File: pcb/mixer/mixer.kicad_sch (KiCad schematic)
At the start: 17 parts, among them J1 Conn_01x02_Pin, J4 Conn_Coaxial, J5 Conn_Coaxial, J6 AudioJack3, J7 AudioJack3, P1 PMOD-Device-x2-Type-Generic-A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, U17 LT1117-3.3, U3 Si5351C-B-GU, U5 LT1117-5.0, X8 TCXO-14

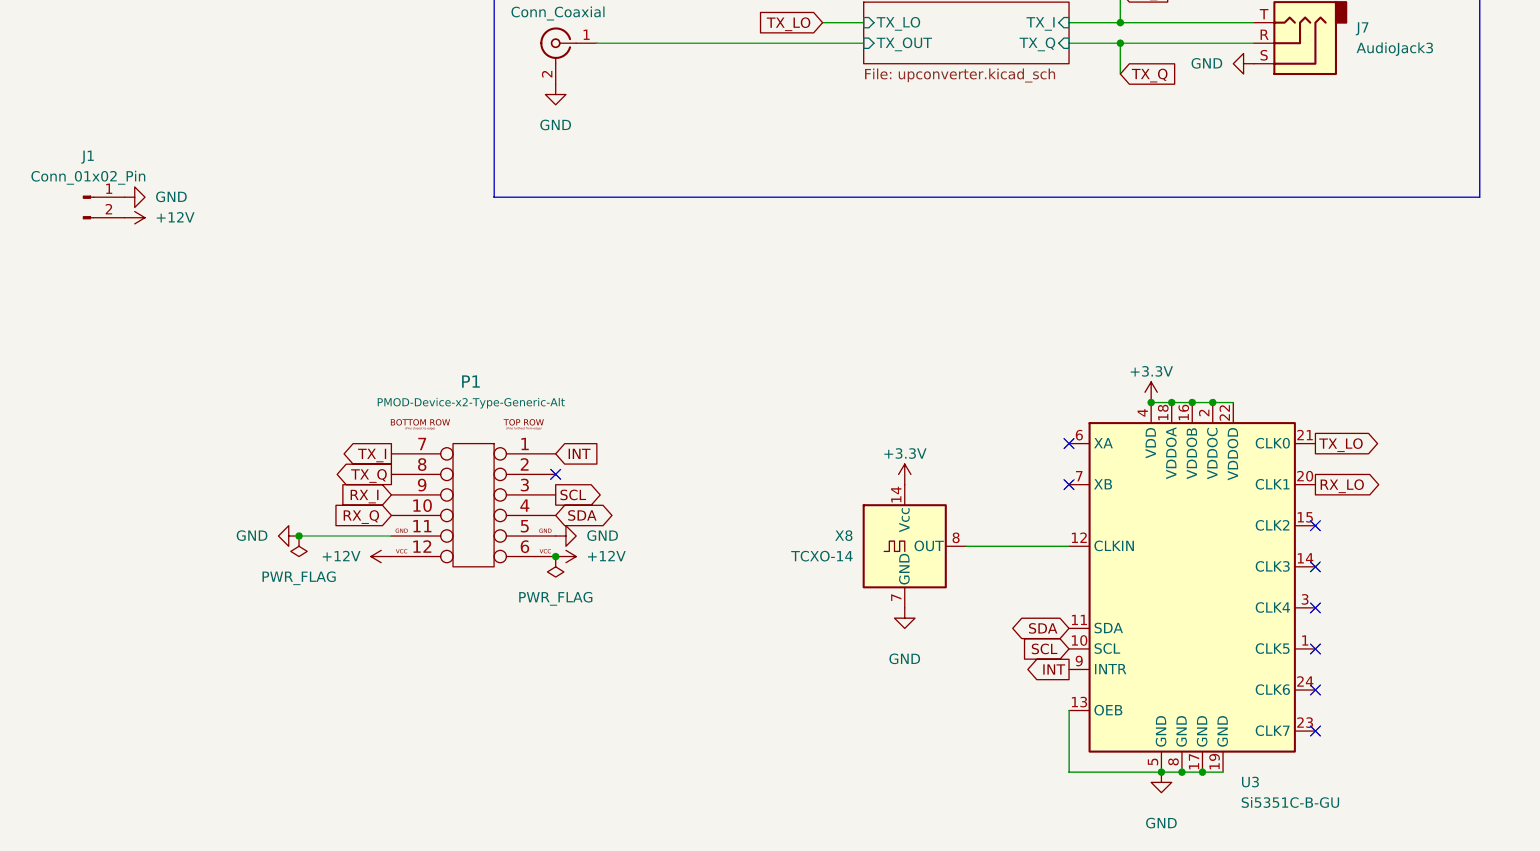
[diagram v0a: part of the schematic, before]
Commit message: add README.md from external repository
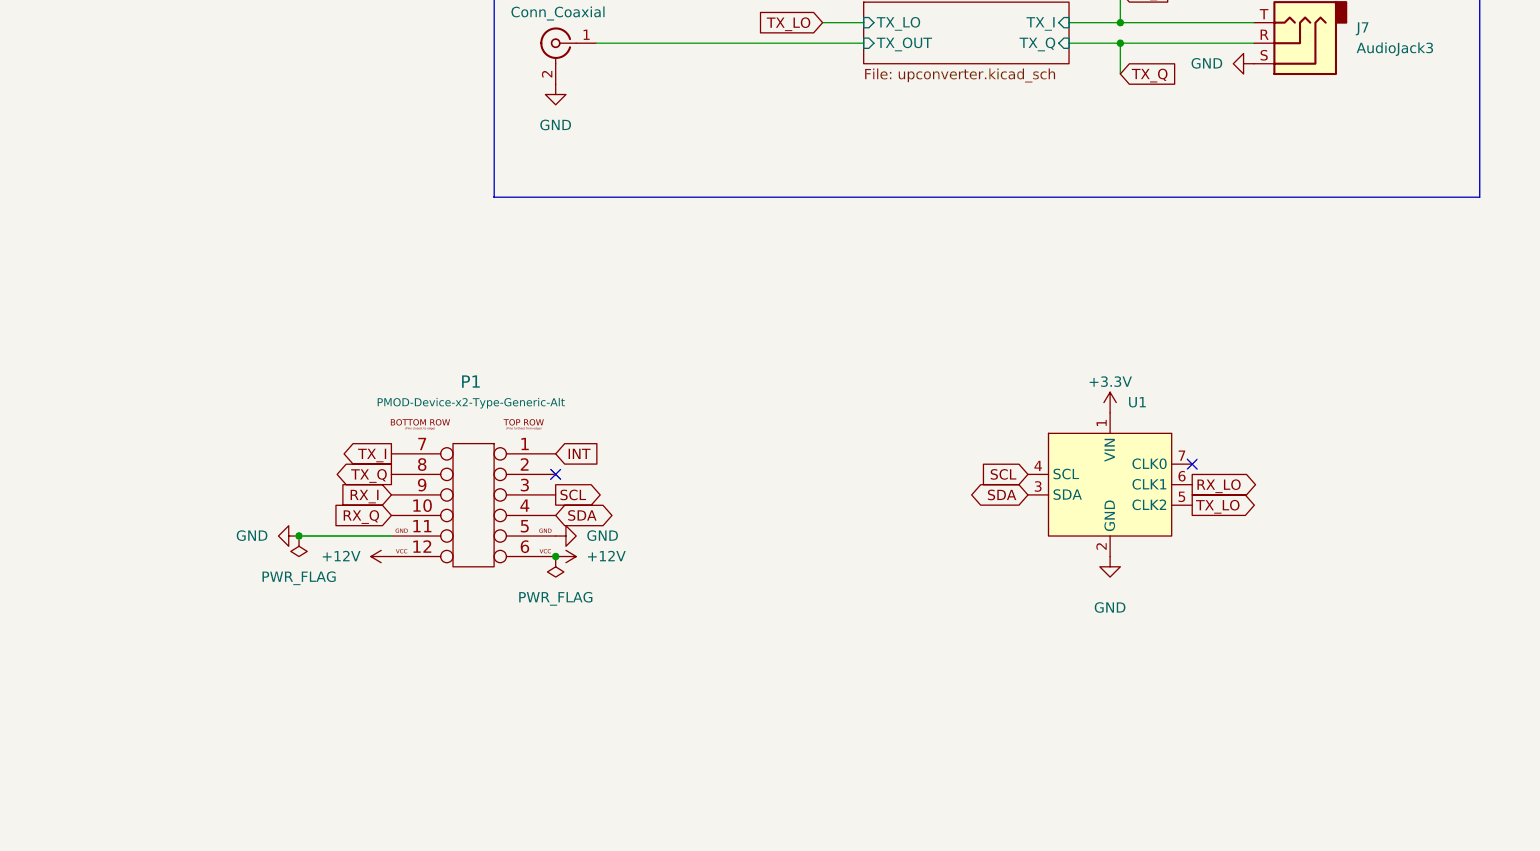
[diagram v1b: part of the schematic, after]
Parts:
- removed J1: Conn_01x02_Pin, Connector_JST:JST_VH_S2P-VH_1x02_P3.96mm_Horizontal, symbol Connector:Conn_01x02_Pin
- removed U3: Si5351C-B-GU, Package_SO:QSOP-24_3.9x8.7mm_P0.635mm, symbol pico-sdx:Si5351C-B-GU
- removed X8: TCXO-14, Oscillator:Oscillator_DIP-14, symbol Oscillator:TCXO-14
- added U1: ~, pico-sdx:Module_Si5351, symbol pico-sdx:Si5351A_Clock_Generator_Breakout_
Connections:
- net +3.3V: now also U1.1 (VIN)
- net GND: now also U1.2 (GND)
- net RX_LO: now also U1.6 (CLK1)
- net SCL: now also U1.4 (SCL)
- net SDA: now also U1.3 (SDA)
- net TX_LO: now also U1.5 (CLK2)
- no-connect marks 9 -> 2
